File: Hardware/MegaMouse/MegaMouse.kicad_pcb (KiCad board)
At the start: 2 copper layers, 93.1 x 158.2 mm, 127 parts, among them J101 SHIFT_CONN, J102 PROG_CONN, J103 SHIFT_CONN, J104 PROG_CONN, J201 Motor, J301 Motor, J401 ICSP, J601 USBC, SW401 RESET, SW402 START/MODE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

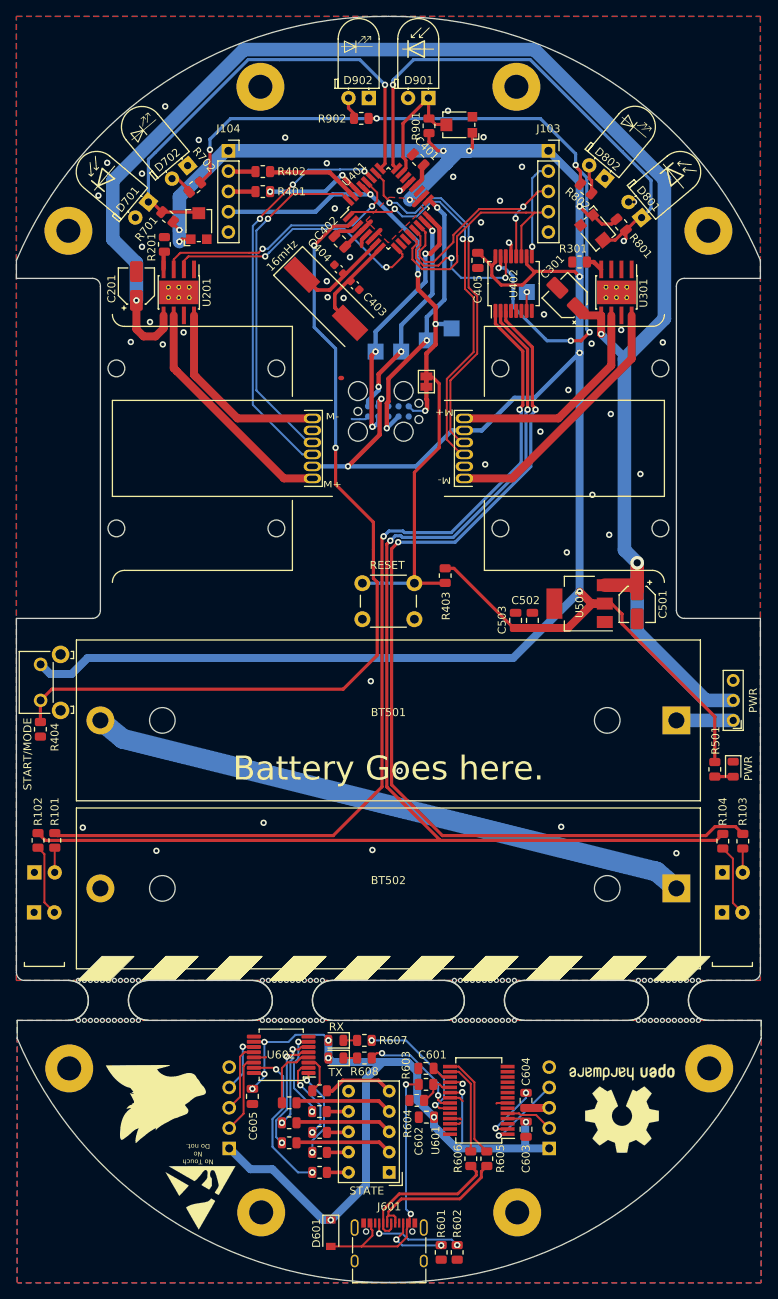
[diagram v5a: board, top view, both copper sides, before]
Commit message: Fix DRC and prep for a v1.0 release!
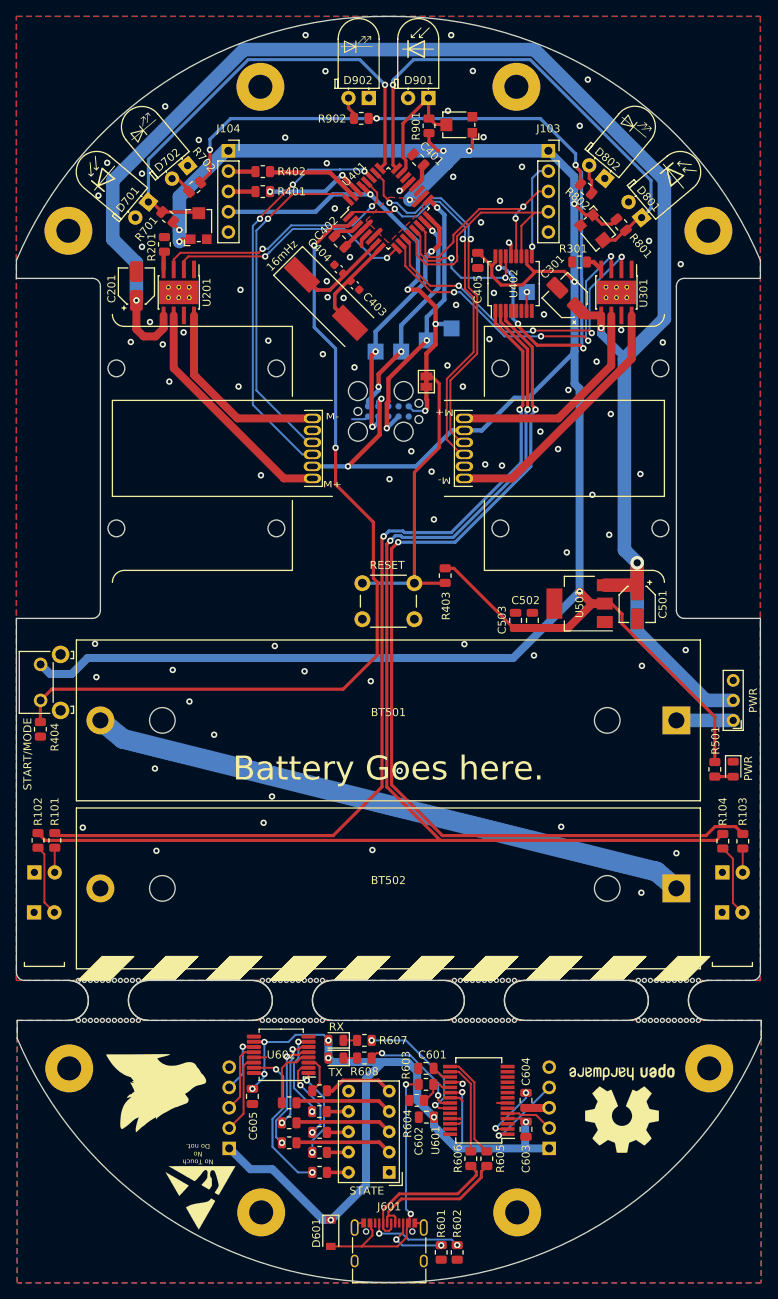
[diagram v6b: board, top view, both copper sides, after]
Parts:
- removed the G*** at (-29.0, 82.0)
- removed the G*** at (-17.8, 27.9)
- added G***: LOGO, KenwoodFox:KITSUNE_LOGO, F.Cu at (-29.0, 80.6)
- added G***: LOGO, MegaMouse:JLCPCB, B.Cu at (-22.9, -6.89)
- added G***: LOGO, KenwoodFox:KITSUNE_LOGO, B.Cu at (-17.9, 27.8)
- added SNHU_NEW***: LOGO, KenwoodFox:SNHU_NEW, B.Cu at (-23.6, 2.71)
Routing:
- net /MCU/R_MOT_1: track 0.00 -> 43.3 mm, vias 0 -> 4
- net /MCU/R_MOT_2: track 0.00 -> 42.7 mm, vias 0 -> 4
- net /LeftMotor/IN2: track 33.9 -> 31.3 mm
- net GND: track 20.2 -> 22.5 mm, vias 47 -> 86
- net /ENABLE: track 100.5 -> 102.5 mm
- net /MCU/RST: track 86.7 -> 88.5 mm
- net /MCU/LATCH: track 31.7 -> 30.0 mm
- net /MCU/CLOCK: track 32.2 -> 30.5 mm
- net /MCU/DATA: track 20.4 -> 18.8 mm
- net /RIR: track 63.3 -> 61.9 mm, vias 2 -> 1
- net /MCU/SDO: track 26.9 -> 27.5 mm
- net +5V: track 448.4 -> 448.3 mm, vias 20 -> 19
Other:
- board text added: "Git Revision"
- board text added: "JLCJLCJLCJLC"

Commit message: Carlstrom Review (#2)
Thank you to Professor Carlstrom for reviewing!
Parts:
- added H701: Screw Adjust Hole, MountingHole:MountingHole_3mm, F.Cu at (23.8, 78.2)
- added H801: Screw Adjust Hole, MountingHole:MountingHole_3mm, F.Cu at (-25.9, 77.5)
- added H901: Screw Adjust Hole, MountingHole:MountingHole_3mm, F.Cu at (-8.70, 91.3)
- added REF**: KiCad-Logo_5mm_SilkScreen, Symbol:KiCad-Logo_5mm_SilkScreen, F.Cu at (28.8, 86.6)
- moved REF** 4.14 mm to (30.6, 78.6)
- moved R609 3.63 mm to (-12.2, 90.0)
- moved G*** 3.27 mm to (-29.8, 83.8)
- turned H101 to 180 degrees
- renumbered TP406 to TP405
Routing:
- net /Upper Board/SEG_A: track 2.71 -> 7.08 mm
- net Net-(R609-Pad1): track 19.8 -> 16.7 mm
- net Net-(R401-Pad1): track 12.7 -> 12.1 mm
- net GND: vias 86 -> 103
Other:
- outline, holes or cut-outs redrawn
- board text added: "Stencil Cut Size"
